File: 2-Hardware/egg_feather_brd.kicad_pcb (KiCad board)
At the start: 2 copper layers, 5 parts, among them SW1 SWITCH_SPST, U1 ADAFRUIT_FEATHER, U2 LIS3DH_BOB

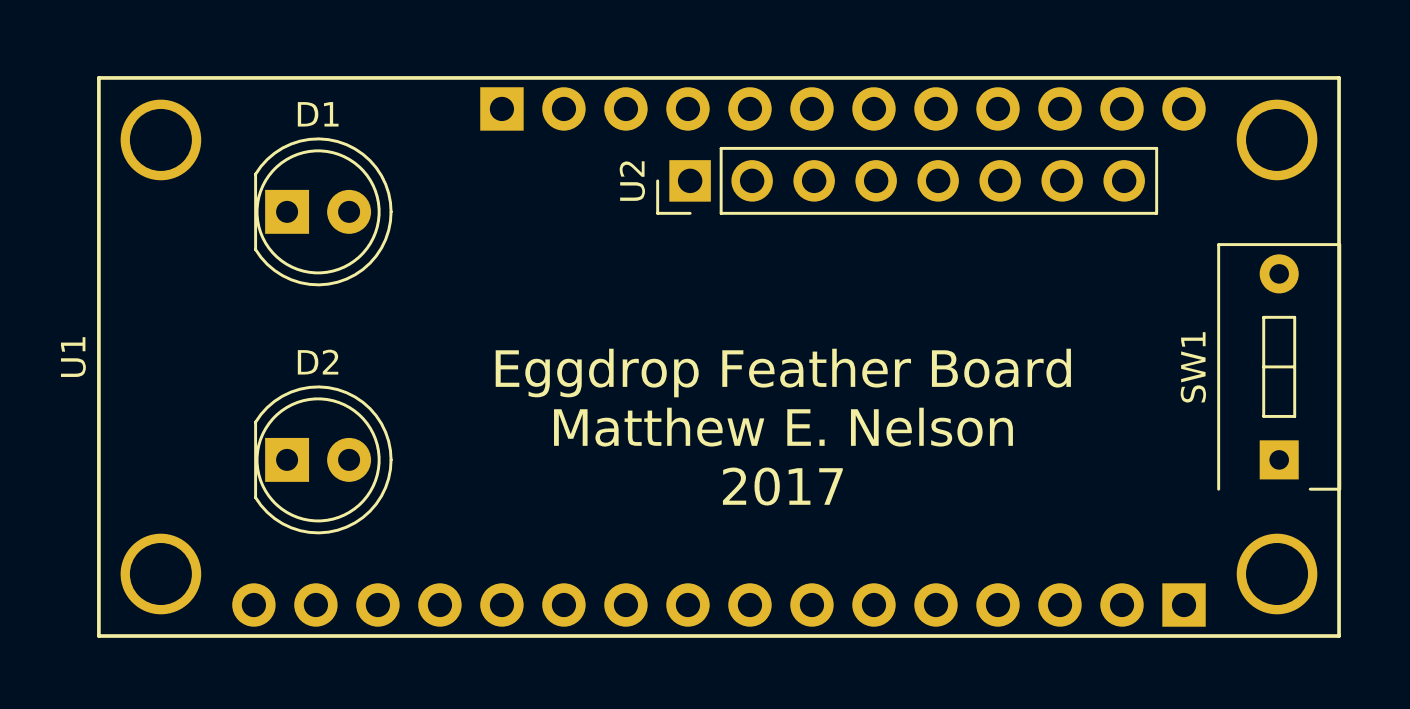
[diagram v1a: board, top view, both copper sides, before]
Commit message: Final revisions to board, routed
Final design for first run.  Board routed and sent to manufacturing.
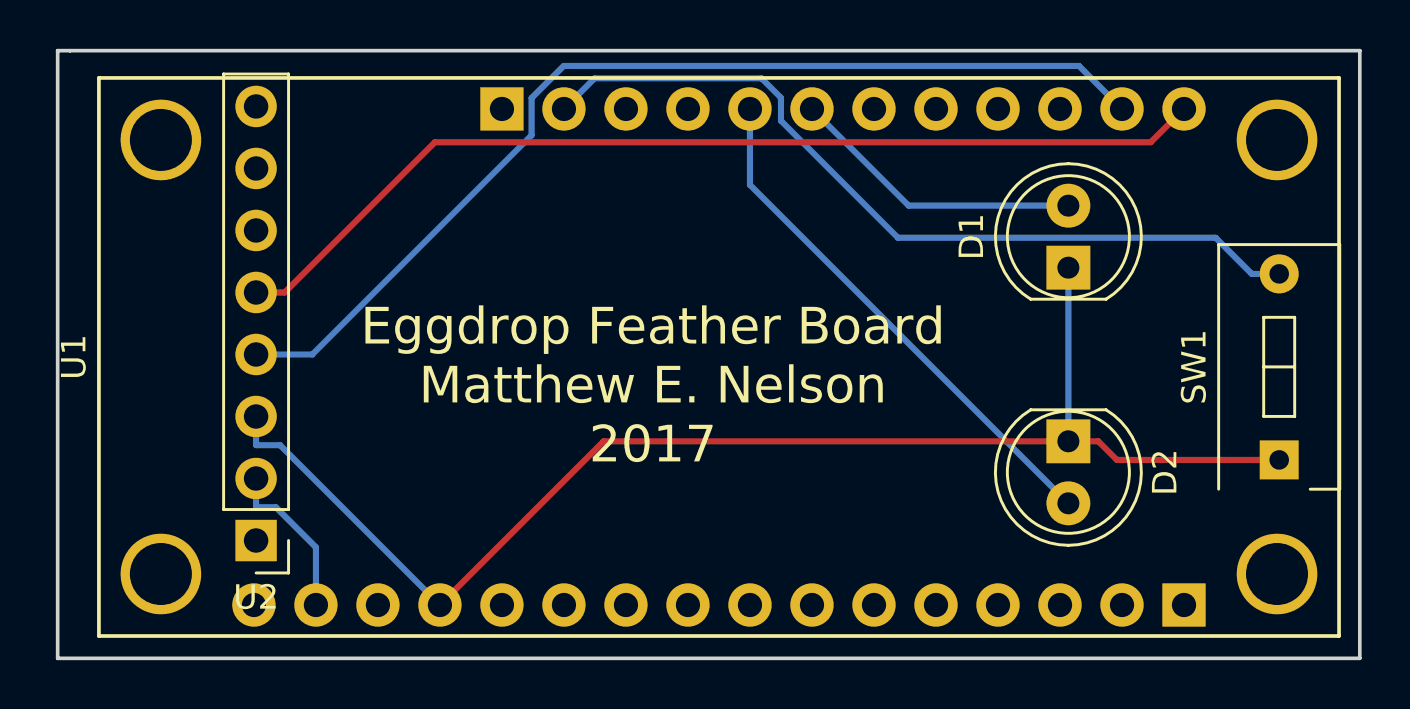
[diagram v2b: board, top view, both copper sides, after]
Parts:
- moved D1 32.1 mm to (162.8, 101.3), turned to 90 degrees
- moved D2 32.0 mm to (162.8, 108.5), turned to 270 degrees
- moved U2 23.1 mm to (129.5, 112.5), turned to 180 degrees
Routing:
- net Net-(D1-Pad1): track 0.00 -> 56.0 mm
- net Net-(U1-Pad27): track 0.00 -> 42.0 mm
- net Net-(U1-Pad28): track 0.00 -> 41.1 mm
- net Net-(SW1-Pad2): track 0.00 -> 33.7 mm
- net Net-(D2-Pad2): track 0.00 -> 21.6 mm
- net Net-(D1-Pad2): track 0.00 -> 12.1 mm
- net Net-(U1-Pad15): track 0.00 -> 6.67 mm
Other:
- board outline added: 53.3 x 24.9 mm
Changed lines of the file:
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@@
   (general
     (links 10)
-    (no_connects 10)
-    (area 121.06 93.298999 176.005 116.709001)
+    (no_connects 0)
+    (area 121.336999 92.380999 174.827001 117.423001)
     (thickness 1.6)
-    (drawings 1)
-    (tracks 0)
+    (drawings 6)
+    (tracks 35)
     (zones 0)
     (modules 5)
@@
     (pad_to_mask_clearance 0.2)
     (aux_axis_origin 0 0)
-    (visible_elements FFFFFF7F)
+    (visible_elements 7FFFFFFF)
     (pcbplotparams
       (layerselection 0x00030_80000001)
@@
   )
   (module LEDs:LED_D5.0mm (layer F.Cu)
-    (at 130.81 99.06)
+    (at 162.814 101.346 90)
     (descr "LED, diameter 5.0mm, 2 pins, http://cdn-reichelt.de/documents/datenblatt/A500/LL-504BC2E-009.pdf")
     (tags "LED diameter 5.0mm 2 pins")
-    (fp_text reference D1 (at 1.27 -3.96) (layer F.SilkS)
-      (effects (font (size 1 1) (thickness 0.15)))
-    )
-    (fp_text value LED (at 1.27 3.96) (layer F.Fab)
+    (fp_text reference D1 (at 1.27 -3.96 90) (layer F.SilkS)
+      (effects (font (size 1 1) (thickness 0.15)))
+    )
+    (fp_text value LED (at 1.27 3.96 90) (layer F.Fab)
       (effects (font (size 1 1) (thickness 0.15)))
     )
@@
     (fp_line (start 4.5 3.25) (end 4.5 -3.25) (layer F.CrtYd) (width 0.05))
     (fp_line (start 4.5 -3.25) (end -1.95 -3.25) (layer F.CrtYd) (width 0.05))
-    (pad 1 thru_hole rect (at 0 0) (size 1.8 1.8) (drill 0.9) (layers *.Cu *.Mask)
-      (net 1 "Net-(D1-Pad1)"))
-    (pad 2 thru_hole circle (at 2.54 0) (size 1.8 1.8) (drill 0.9) (layers *.Cu *.Mask)
+    (pad 1 thru_hole rect (at 0 0 90) (size 1.8 1.8) (drill 0.9) (layers *.Cu *.Mask)
+      (net 1 "Net-(D1-Pad1)"))
+    (pad 2 thru_hole circle (at 2.54 0 90) (size 1.8 1.8) (drill 0.9) (layers *.Cu *.Mask)
       (net 2 "Net-(D1-Pad2)"))
     (model LEDs.3dshapes/LED_D5.0mm.wrl
@@
   )
   (module LEDs:LED_D5.0mm (layer F.Cu)
-    (at 130.81 109.22)
+    (at 162.814 108.458 270)
     (descr "LED, diameter 5.0mm, 2 pins, http://cdn-reichelt.de/documents/datenblatt/A500/LL-504BC2E-009.pdf")
     (tags "LED diameter 5.0mm 2 pins")
-    (fp_text reference D2 (at 1.27 -3.96) (layer F.SilkS)
-      (effects (font (size 1 1) (thickness 0.15)))
-    )
-    (fp_text value LED (at 1.27 3.96) (layer F.Fab)
+    (fp_text reference D2 (at 1.27 -3.96 270) (layer F.SilkS)
+      (effects (font (size 1 1) (thickness 0.15)))
+    )
+    (fp_text value LED (at 1.27 3.96 270) (layer F.Fab)
       (effects (font (size 1 1) (thickness 0.15)))
     )
@@
     (fp_line (start 4.5 3.25) (end 4.5 -3.25) (layer F.CrtYd) (width 0.05))
     (fp_line (start 4.5 -3.25) (end -1.95 -3.25) (layer F.CrtYd) (width 0.05))
-    (pad 1 thru_hole rect (at 0 0) (size 1.8 1.8) (drill 0.9) (layers *.Cu *.Mask)
-      (net 1 "Net-(D1-Pad1)"))
-    (pad 2 thru_hole circle (at 2.54 0) (size 1.8 1.8) (drill 0.9) (layers *.Cu *.Mask)
+    (pad 1 thru_hole rect (at 0 0 270) (size 1.8 1.8) (drill 0.9) (layers *.Cu *.Mask)
+      (net 1 "Net-(D1-Pad1)"))
+    (pad 2 thru_hole circle (at 2.54 0 270) (size 1.8 1.8) (drill 0.9) (layers *.Cu *.Mask)
       (net 3 "Net-(D2-Pad2)"))
     (model LEDs.3dshapes/LED_D5.0mm.wrl
@@
   )
   (module Pin_Headers:Pin_Header_Straight_1x08_Pitch2.54mm (layer F.Cu)
-    (at 147.32 97.79 90)
+    (at 129.54 112.522 180)
     (descr "Through hole straight pin header, 1x08, 2.54mm pitch, single row")
     (tags "Through hole pin header THT 1x08 2.54mm single row")
-    (fp_text reference U2 (at 0 -2.33 90) (layer F.SilkS)
-      (effects (font (size 1 1) (thickness 0.15)))
-    )
-    (fp_text value LIS3DH_BOB (at -2.794 14.732 180) (layer F.Fab)
+    (fp_text reference U2 (at 0 -2.33 180) (layer F.SilkS)
+      (effects (font (size 1 1) (thickness 0.15)))
+    )
+    (fp_text value LIS3DH_BOB (at -2.794 14.732 270) (layer F.Fab)
       (effects (font (size 1 1) (thickness 0.15)))
     )
@@
     (fp_line (start 1.8 19.55) (end 1.8 -1.8) (layer F.CrtYd) (width 0.05))
     (fp_line (start 1.8 -1.8) (end -1.8 -1.8) (layer F.CrtYd) (width 0.05))
-    (fp_text user %R (at 0 -2.33 90) (layer F.Fab)
-      (effects (font (size 1 1) (thickness 0.15)))
-    )
-    (pad 1 thru_hole rect (at 0 0 90) (size 1.7 1.7) (drill 1) (layers *.Cu *.Mask))
-    (pad 2 thru_hole oval (at 0 2.54 90) (size 1.7 1.7) (drill 1) (layers *.Cu *.Mask)
+    (fp_text user %R (at 0 -2.33 180) (layer F.Fab)
+      (effects (font (size 1 1) (thickness 0.15)))
+    )
+    (pad 1 thru_hole rect (at 0 0 180) (size 1.7 1.7) (drill 1) (layers *.Cu *.Mask))
+    (pad 2 thru_hole oval (at 0 2.54 180) (size 1.7 1.7) (drill 1) (layers *.Cu *.Mask)
       (net 5 "Net-(U1-Pad15)"))
-    (pad 3 thru_hole oval (at 0 5.08 90) (size 1.7 1.7) (drill 1) (layers *.Cu *.Mask)
-      (net 1 "Net-(D1-Pad1)"))
-    (pad 4 thru_hole oval (at 0 7.62 90) (size 1.7 1.7) (drill 1) (layers *.Cu *.Mask)
+    (pad 3 thru_hole oval (at 0 5.08 180) (size 1.7 1.7) (drill 1) (layers *.Cu *.Mask)
+      (net 1 "Net-(D1-Pad1)"))
+    (pad 4 thru_hole oval (at 0 7.62 180) (size 1.7 1.7) (drill 1) (layers *.Cu *.Mask)
       (net 6 "Net-(U1-Pad27)"))
-    (pad 5 thru_hole oval (at 0 10.16 90) (size 1.7 1.7) (drill 1) (layers *.Cu *.Mask)
+    (pad 5 thru_hole oval (at 0 10.16 180) (size 1.7 1.7) (drill 1) (layers *.Cu *.Mask)
       (net 7 "Net-(U1-Pad28)"))
-    (pad 6 thru_hole oval (at 0 12.7 90) (size 1.7 1.7) (drill 1) (layers *.Cu *.Mask))
-    (pad 7 thru_hole oval (at 0 15.24 90) (size 1.7 1.7) (drill 1) (layers *.Cu *.Mask))
-    (pad 8 thru_hole oval (at 0 17.78 90) (size 1.7 1.7) (drill 1) (layers *.Cu *.Mask))
+    (pad 6 thru_hole oval (at 0 12.7 180) (size 1.7 1.7) (drill 1) (layers *.Cu *.Mask))
+    (pad 7 thru_hole oval (at 0 15.24 180) (size 1.7 1.7) (drill 1) (layers *.Cu *.Mask))
+    (pad 8 thru_hole oval (at 0 17.78 180) (size 1.7 1.7) (drill 1) (layers *.Cu *.Mask))
     (model ${KISYS3DMOD}/Pin_Headers.3dshapes/Pin_Header_Straight_1x08_Pitch2.54mm.wrl
       (at (xyz 0 -0.35 0))
@@
     )
   )
-  (gr_text "Eggdrop Feather Board\nMatthew E. Nelson\n2017" (at 151.13 107.95) (layer F.SilkS)
+  (gr_line (start 121.412 92.456) (end 121.92 92.456) (angle 90) (layer Edge.Cuts) (width 0.15))
+  (gr_line (start 121.412 117.348) (end 121.412 92.456) (angle 90) (layer Edge.Cuts) (width 0.15))
+  (gr_line (start 174.752 117.348) (end 121.412 117.348) (angle 90) (layer Edge.Cuts) (width 0.15))
+  (gr_line (start 174.752 92.456) (end 174.752 117.348) (angle 90) (layer Edge.Cuts) (width 0.15))
+  (gr_line (start 121.92 92.456) (end 174.752 92.456) (angle 90) (layer Edge.Cuts) (width 0.15))
+  (gr_text "Eggdrop Feather Board\nMatthew E. Nelson\n2017" (at 145.796 106.172) (layer F.SilkS)
     (effects (font (size 1.5 1.5) (thickness 0.3)))
   )
+  (segment (start 130.5243 108.6173) (end 137.071 115.164) (width 0.25) (layer B.Cu) (net 1))
+  (segment (start 129.54 108.6173) (end 130.5243 108.6173) (width 0.25) (layer B.Cu) (net 1))
+  (segment (start 129.54 107.442) (end 129.54 108.6173) (width 0.25) (layer B.Cu) (net 1))
+  (segment (start 143.777 108.458) (end 162.814 108.458) (width 0.25) (layer F.Cu) (net 1))
+  (segment (start 137.071 115.164) (end 143.777 108.458) (width 0.25) (layer F.Cu) (net 1))
+  (segment (start 164.8013 109.22) (end 164.0393 108.458) (width 0.25) (layer F.Cu) (net 1))
+  (segment (start 171.45 109.22) (end 164.8013 109.22) (width 0.25) (layer F.Cu) (net 1))
+  (segment (start 162.814 108.458) (end 164.0393 108.458) (width 0.25) (layer F.Cu) (net 1))
+  (segment (start 162.814 108.458) (end 162.814 101.346) (width 0.25) (layer B.Cu) (net 1))
+  (segment (start 156.273 98.806) (end 152.311 94.844) (width 0.25) (layer B.Cu) (net 2))
+  (segment (start 162.814 98.806) (end 156.273 98.806) (width 0.25) (layer B.Cu) (net 2))
+  (segment (start 149.771 97.955) (end 162.814 110.998) (width 0.25) (layer B.Cu) (net 3))
+  (segment (start 149.771 94.844) (end 149.771 97.955) (width 0.25) (layer B.Cu) (net 3))
+  (segment (start 168.8453 100.1206) (end 170.3247 101.6) (width 0.25) (layer B.Cu) (net 4))
+  (segment (start 155.8349 100.1206) (end 168.8453 100.1206) (width 0.25) (layer B.Cu) (net 4))
+  (segment (start 151.041 95.3267) (end 155.8349 100.1206) (width 0.25) (layer B.Cu) (net 4))
+  (segment (start 151.041 94.3859) (end 151.041 95.3267) (width 0.25) (layer B.Cu) (net 4))
+  (segment (start 150.2435 93.5884) (end 151.041 94.3859) (width 0.25) (layer B.Cu) (net 4))
+  (segment (start 143.4066 93.5884) (end 150.2435 93.5884) (width 0.25) (layer B.Cu) (net 4))
+  (segment (start 142.151 94.844) (end 143.4066 93.5884) (width 0.25) (layer B.Cu) (net 4))
+  (segment (start 171.45 101.6) (end 170.3247 101.6) (width 0.25) (layer B.Cu) (net 4))
+  (segment (start 131.991 112.8003) (end 131.991 115.164) (width 0.25) (layer B.Cu) (net 5))
+  (segment (start 130.348 111.1573) (end 131.991 112.8003) (width 0.25) (layer B.Cu) (net 5))
+  (segment (start 129.54 111.1573) (end 130.348 111.1573) (width 0.25) (layer B.Cu) (net 5))
+  (segment (start 129.54 109.982) (end 129.54 111.1573) (width 0.25) (layer B.Cu) (net 5))
+  (segment (start 163.2494 93.0824) (end 165.011 94.844) (width 0.25) (layer B.Cu) (net 6))
+  (segment (start 142.1396 93.0824) (end 163.2494 93.0824) (width 0.25) (layer B.Cu) (net 6))
+  (segment (start 140.8254 94.3966) (end 142.1396 93.0824) (width 0.25) (layer B.Cu) (net 6))
+  (segment (start 140.8254 95.9189) (end 140.8254 94.3966) (width 0.25) (layer B.Cu) (net 6))
+  (segment (start 131.8423 104.902) (end 140.8254 95.9189) (width 0.25) (layer B.Cu) (net 6))
+  (segment (start 129.54 104.902) (end 131.8423 104.902) (width 0.25) (layer B.Cu) (net 6))
+  (segment (start 166.1875 96.2075) (end 167.551 94.844) (width 0.25) (layer F.Cu) (net 7))
+  (segment (start 136.8698 96.2075) (end 166.1875 96.2075) (width 0.25) (layer F.Cu) (net 7))
+  (segment (start 130.7153 102.362) (end 136.8698 96.2075) (width 0.25) (layer F.Cu) (net 7))
+  (segment (start 129.54 102.362) (end 130.7153 102.362) (width 0.25) (layer F.Cu) (net 7))
 )

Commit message: Changed LEDs
Changed to surface mount LEDs
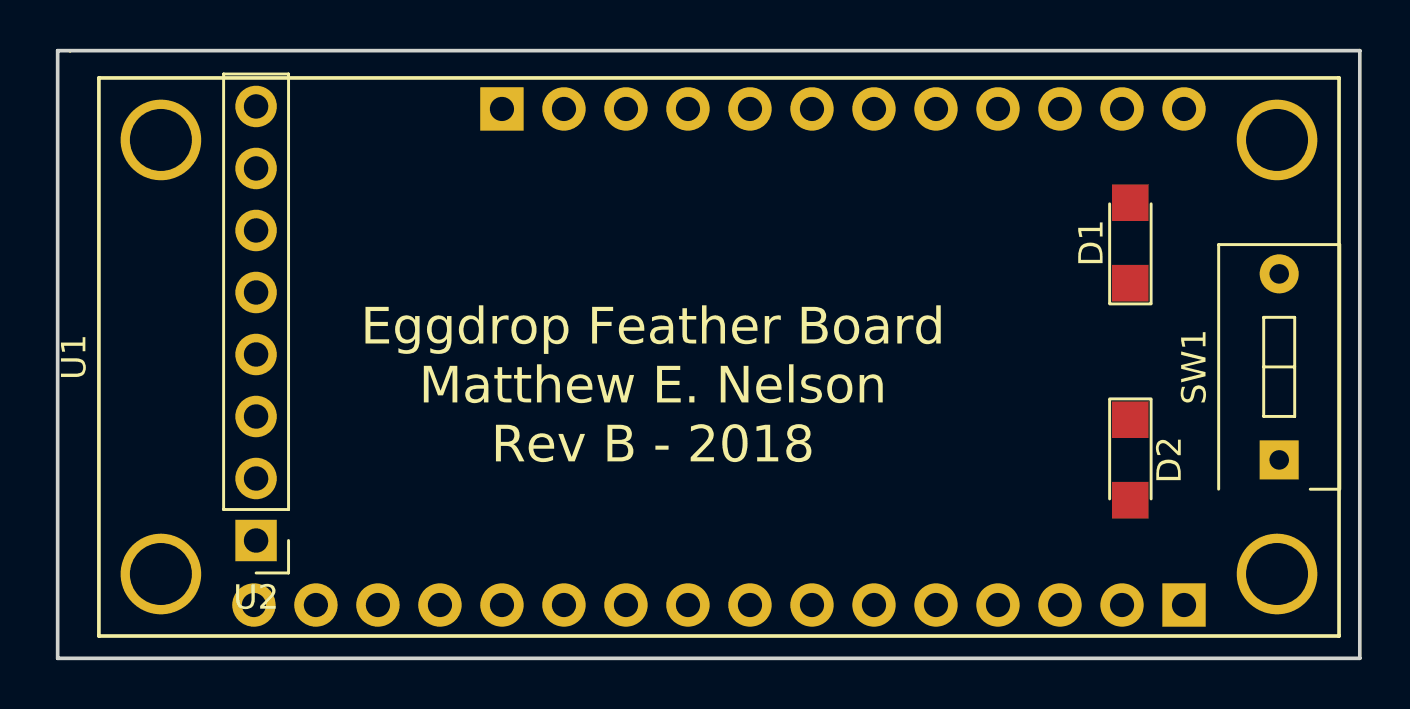
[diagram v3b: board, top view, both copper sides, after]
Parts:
- D1, D2: footprint LEDs:LED_D5.0mm -> LEDs:LED_1206
- moved D1 2.74 mm to (165.4, 100.3)
- moved D2 2.65 mm to (165.4, 109.2)
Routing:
- net Net-(D1-Pad1): track 56.0 -> 0.00 mm
- net Net-(U1-Pad27): track 42.0 -> 0.00 mm
- net Net-(U1-Pad28): track 41.1 -> 0.00 mm
- net Net-(SW1-Pad2): track 33.7 -> 0.00 mm
- net Net-(D2-Pad2): track 21.6 -> 0.00 mm
- net Net-(D1-Pad2): track 12.1 -> 0.00 mm
- net Net-(U1-Pad15): track 6.67 -> 0.00 mm
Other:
- board text added: "Eggdrop Feather Board Matthew E. Nelson Rev B - 2018"
- board text removed: "Eggdrop Feather Board Matthew E. Nelson 2017"
